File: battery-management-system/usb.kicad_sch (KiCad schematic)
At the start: 2 parts

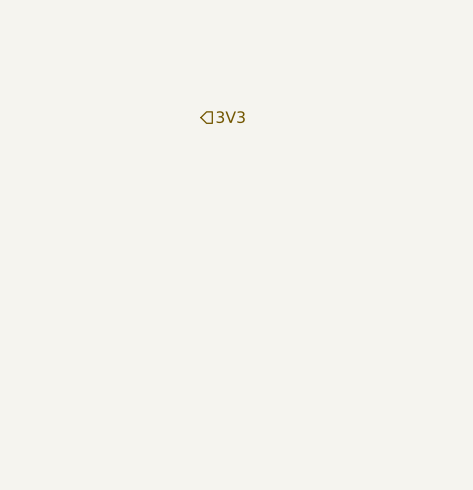
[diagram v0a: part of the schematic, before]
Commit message: define basic hierarchy and power supplies
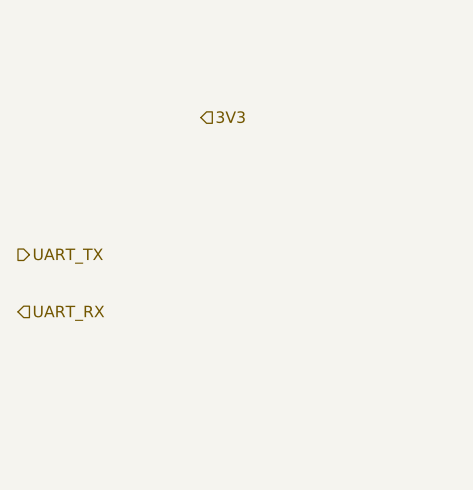
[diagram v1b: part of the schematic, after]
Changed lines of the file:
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@@
 (kicad_sch (version 20211123) (generator eeschema)
   (paper "A4")
+  (hierarchical_label "UART_TX" (shape output) (at 78.74 77.47 0)
+    (effects (font (size 1.27 1.27)) (justify left))
+  )
+  (hierarchical_label "UART_RX" (shape input) (at 78.74 83.82 0)
+    (effects (font (size 1.27 1.27)) (justify left))
+  )
   (hierarchical_label "5V_USB" (shape output) (at 99.06 45.72 0)
     (effects (font (size 1.27 1.27)) (justify left))

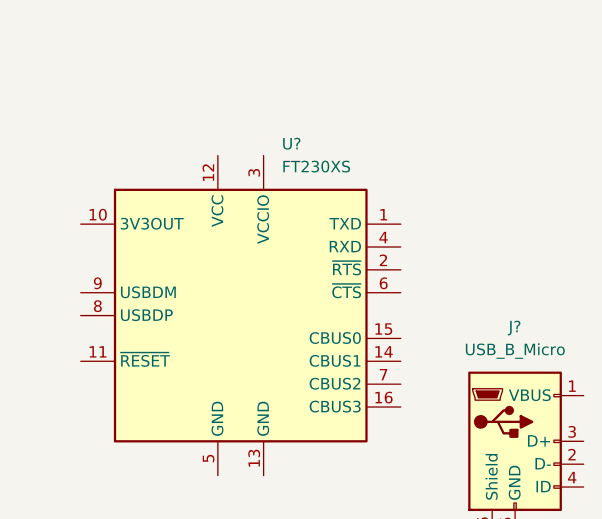
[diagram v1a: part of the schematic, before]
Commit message: add RS order numbers
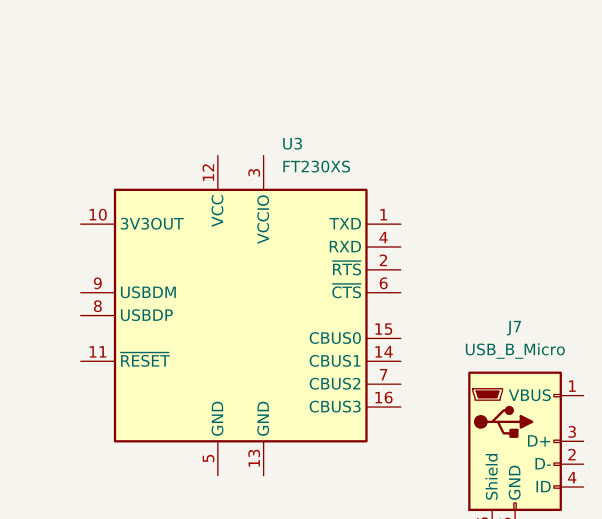
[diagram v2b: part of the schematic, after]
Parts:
- J7: renamed from J?; symbol Connector:USB_B_Micro -> benediktibk:USB_B_Micro
- U3: renamed from U?; symbol Interface_USB:FT230XS -> benediktibk:FT230XS
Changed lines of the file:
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@@
     (effects (font (size 1.27 1.27)) (justify left))
   )
-  (symbol (lib_id "Interface_USB:FT230XS") (at 222.25 77.47 0) (unit 1)
+  (symbol (lib_id "benediktibk:FT230XS") (at 222.25 77.47 0) (unit 1)
     (in_bom yes) (on_board yes) (fields_autoplaced)
-    (property "Reference" "U?" (id 0) (at 226.8094 58.42 0)
+    (property "Reference" "U3" (id 0) (at 226.8094 58.42 0)
       (effects (font (size 1.27 1.27)) (justify left))
     )
@@
     (pin "9")
   )
-  (symbol (lib_id "Connector:USB_B_Micro") (at 252.73 91.44 0) (unit 1)
+  (symbol (lib_id "benediktibk:USB_B_Micro") (at 252.73 91.44 0) (unit 1)
     (in_bom yes) (on_board yes) (fields_autoplaced)
-    (property "Reference" "J?" (id 0) (at 252.73 78.74 0))
+    (property "Reference" "J7" (id 0) (at 252.73 78.74 0))
     (property "Value" "USB_B_Micro" (id 1) (at 252.73 81.28 0))
     (property "Footprint" "" (id 2) (at 256.54 92.71 0)

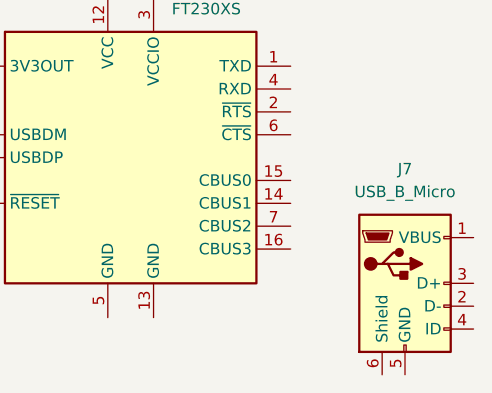
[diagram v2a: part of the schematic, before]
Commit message: add missing order numbers
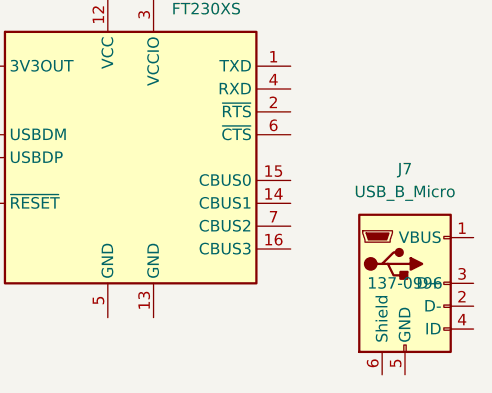
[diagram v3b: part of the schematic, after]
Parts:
- J7: RS order number (none) -> 137-0996
- U3: RS order number (none) -> 757-0010
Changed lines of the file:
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@@
+      (effects (font (size 1.27 1.27)) hide)
+    )
+    (property "RS order number" "757-0010" (id 4) (at 222.25 77.47 0)
       (effects (font (size 1.27 1.27)) hide)
     )
@@
       (effects (font (size 1.27 1.27)) hide)
     )
+    (property "RS order number" "137-0996" (id 4) (at 252.73 91.44 0))
     (pin "1")
     (pin "2")

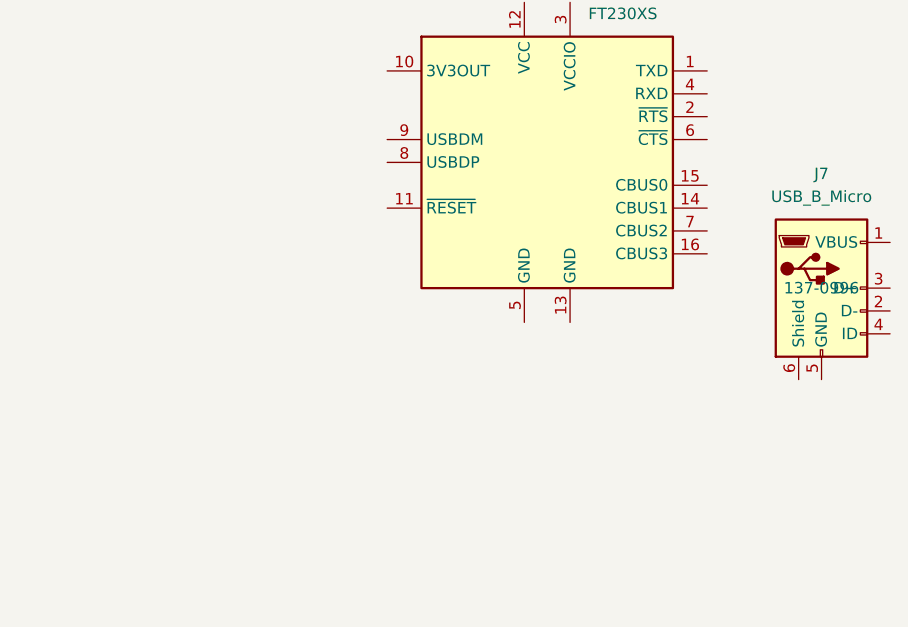
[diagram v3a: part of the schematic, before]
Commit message: use own symbols and footprints
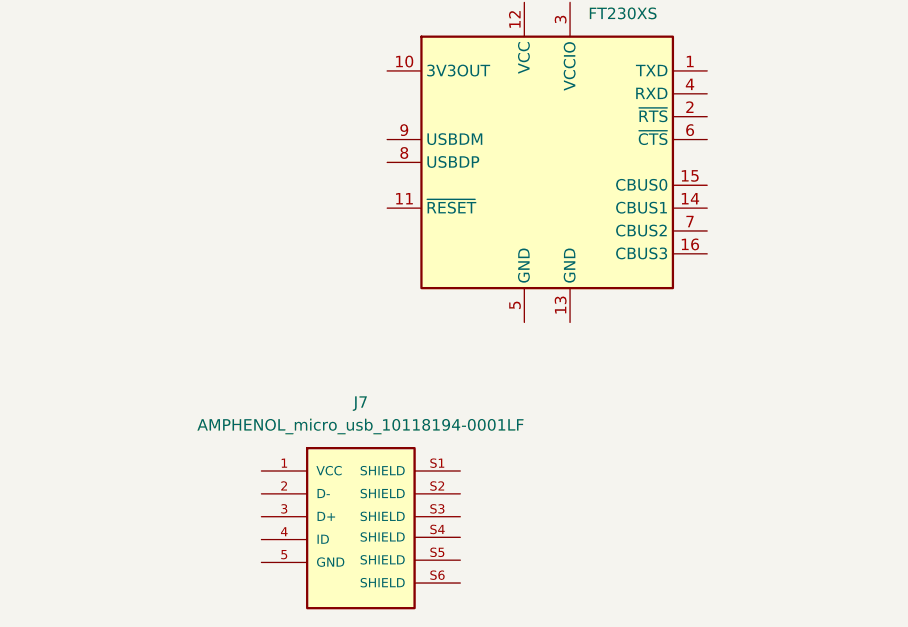
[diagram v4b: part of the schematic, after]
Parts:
- removed J7: USB_B_Micro, symbol benediktibk:USB_B_Micro
- added J7: AMPHENOL_micro_usb_10118194-0001LF, benediktibk:AMPHENOL_10118194-0001LF, symbol benediktibk:AMPHENOL_micro_usb_10118194-0001LF
- U3: footprint Package_SO:SSOP-16_3.9x4.9mm_P0.635mm -> benediktibk:SSOP-16_3.9x4.9mm_P0.635mm
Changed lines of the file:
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@@
       (effects (font (size 1.27 1.27)) (justify left))
     )
-    (property "Footprint" "Package_SO:SSOP-16_3.9x4.9mm_P0.635mm" (id 2) (at 247.65 92.71 0)
+    (property "Footprint" "benediktibk:SSOP-16_3.9x4.9mm_P0.635mm" (id 2) (at 247.65 92.71 0)
       (effects (font (size 1.27 1.27)) hide)
     )
@@
     (pin "9")
   )
-  (symbol (lib_id "benediktibk:USB_B_Micro") (at 252.73 91.44 0) (unit 1)
+  (symbol (lib_id "benediktibk:AMPHENOL_micro_usb_10118194-0001LF") (at 200.66 119.38 0) (unit 1)
     (in_bom yes) (on_board yes) (fields_autoplaced)
-    (property "Reference" "J7" (id 0) (at 252.73 78.74 0))
-    (property "Value" "USB_B_Micro" (id 1) (at 252.73 81.28 0))
-    (property "Footprint" "" (id 2) (at 256.54 92.71 0)
+    (property "Reference" "J7" (id 0) (at 201.549 104.14 0))
+    (property "Value" "AMPHENOL_micro_usb_10118194-0001LF" (id 1) (at 201.549 106.68 0))
+    (property "Footprint" "benediktibk:AMPHENOL_10118194-0001LF" (id 2) (at 201.8792 107.5436 0)
+      (effects (font (size 1.27 1.27)) (justify bottom) hide)
+    )
+    (property "Datasheet" "" (id 3) (at 200.66 119.38 0)
       (effects (font (size 1.27 1.27)) hide)
     )
-    (property "Datasheet" "~" (id 3) (at 256.54 92.71 0)
-      (effects (font (size 1.27 1.27)) hide)
-    )
-    (property "RS order number" "137-0996" (id 4) (at 252.73 91.44 0))
     (pin "1")
     (pin "2")
@@
     (pin "4")
     (pin "5")
-    (pin "6")
+    (pin "S1")
+    (pin "S2")
+    (pin "S3")
+    (pin "S4")
+    (pin "S5")
+    (pin "S6")
   )
 )

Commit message: use M6 connectors, update symbols
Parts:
- J7: RS order number (none) -> 137-0996
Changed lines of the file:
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@@
+      (effects (font (size 1.27 1.27)) hide)
+    )
+    (property "RS order number" "137-0996" (id 4) (at 200.66 119.38 0)
       (effects (font (size 1.27 1.27)) hide)
     )

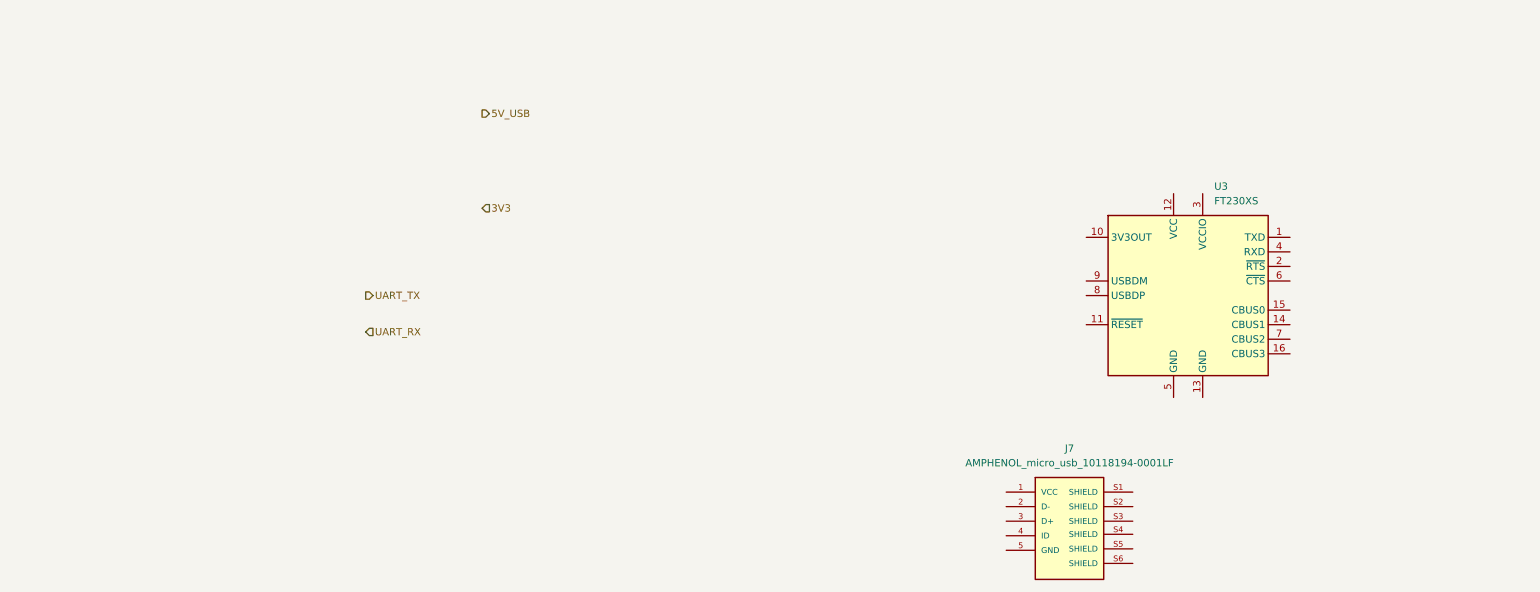
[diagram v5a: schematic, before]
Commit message: create schematic for USB
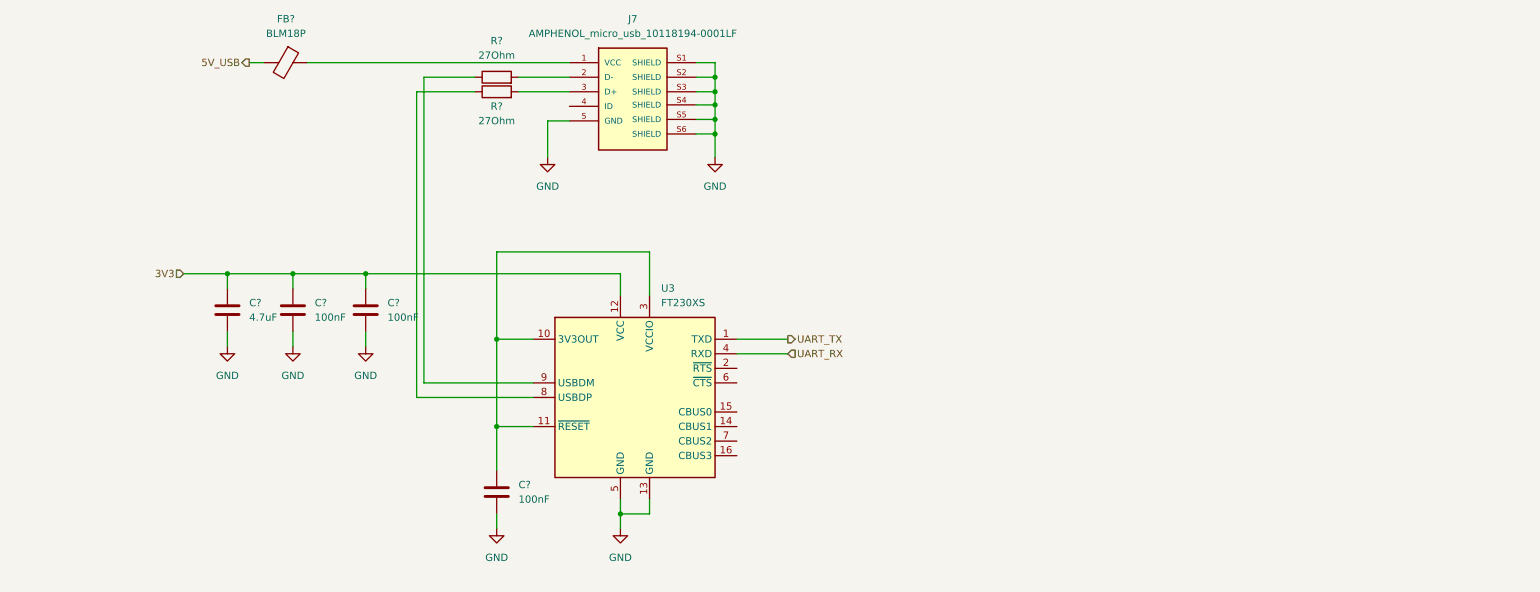
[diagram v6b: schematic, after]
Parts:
- added C? (x3): 100nF, benediktibk:C_0603_1608Metric_Pad1.08x0.95mm_HandSolder, symbol benediktibk:C_100nF_SMD_0603_50V
- added C?: 4.7uF, benediktibk:C_0805_2012Metric_Pad1.18x1.45mm_HandSolder, symbol benediktibk:C_4_7uF_SMD_0805_50V_10%
- added FB?: BLM18P, benediktibk:R_0603_1608Metric_Pad0.98x0.95mm_HandSolder, symbol benediktibk:BLM18P
- added R? (x2): 27Ohm, benediktibk:R_0603_1608Metric_Pad0.98x0.95mm_HandSolder, symbol benediktibk:R_27Ohm_SMD_0603_100mW_1%
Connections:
- net 3V3: now also U3.12 (VCC), C?.1, C?.1, C?.1
- net 5V_USB: now also FB?.2
- net UART_RX: now also U3.4 (RXD)
- net UART_TX: now also U3.1 (TXD)
- net at U3.10 (3V3OUT): now also U3.11 (~{RESET}), U3.3 (VCCIO), C?.1
- net GND: now reaches U3.13 (GND)
- net GND: now also J7.5 (GND), J7.S1 (SHIELD), J7.S2 (SHIELD), J7.S3 (SHIELD), J7.S4 (SHIELD), J7.S5 (SHIELD), J7.S6 (SHIELD), U3.5 (GND), C?.2, C?.2, C?.2, C?.2
- net at U3.8 (USBDP): now also R?.1
- net at U3.9 (USBDM): now also R?.1
- net at J7.1 (VCC): now also FB?.1
- net at J7.2 (D-): now also R?.2
- net at J7.3 (D+): now also R?.2
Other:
- moved on the sheet: J7, U3

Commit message: add resistors, capacitors and LEDs
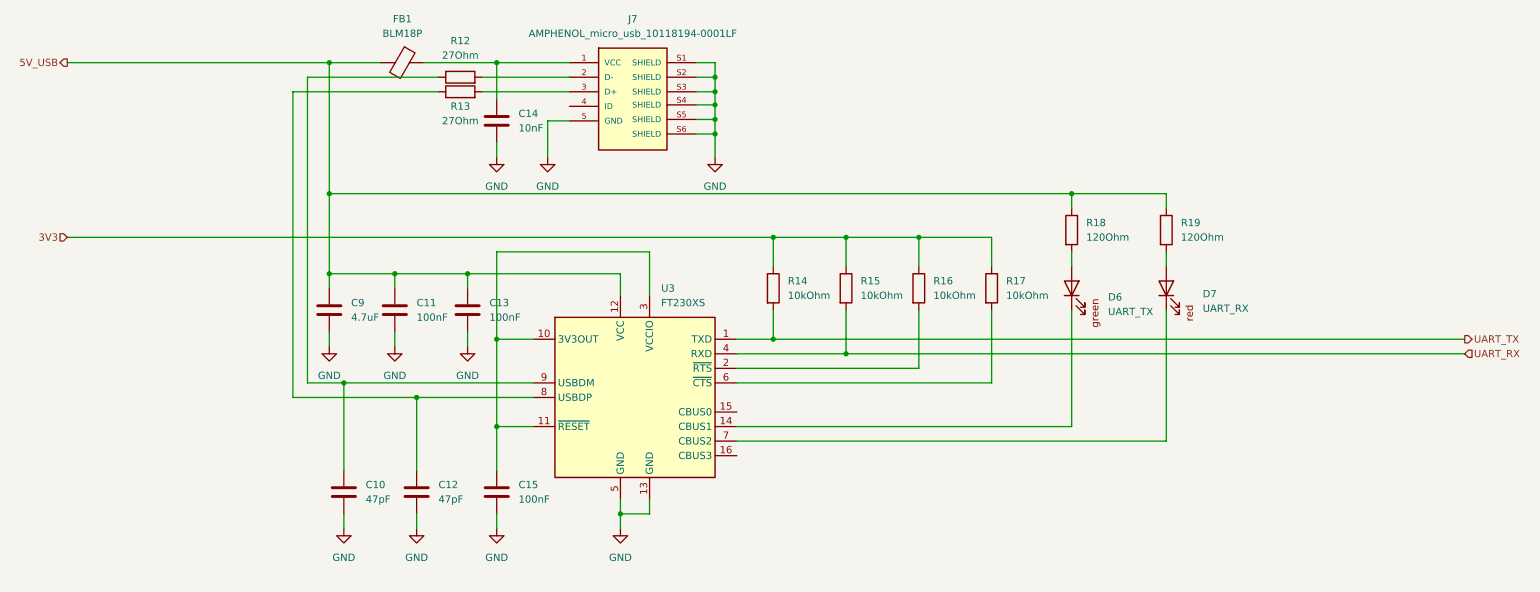
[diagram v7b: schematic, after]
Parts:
- added C10, C12: 47pF, benediktibk:C_0603_1608Metric_Pad1.08x0.95mm_HandSolder, symbol benediktibk:C_47pF_SMD_0603_100V_5%
- added C14: 10nF, benediktibk:C_0603_1608Metric_Pad1.08x0.95mm_HandSolder, symbol benediktibk:C_10nF_SMD_0603_50V_20%
- added D6: UART_TX, benediktibk:D_0603_1608Metric_Pad1.05x0.95mm_HandSolder, symbol benediktibk:LED_green_0603
- added D7: UART_RX, benediktibk:D_0603_1608Metric_Pad1.05x0.95mm_HandSolder, symbol benediktibk:LED_red_0603
- added R14, R15, R16, R17: 10kOhm, benediktibk:R_0603_1608Metric_Pad0.98x0.95mm_HandSolder, symbol benediktibk:R_10kOhm_SMD_0603_100mW_1%
- added R18, R19: 120Ohm, benediktibk:R_0603_1608Metric_Pad0.98x0.95mm_HandSolder, symbol benediktibk:R_120Ohm_SMD_0603_100mW_1%
- gave numbers to parts that had none: 7
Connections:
- net 3V3: now also R14.1, R15.1, R16.1, R17.1; no longer C11.1, C13.1, C9.1, U3.12 (VCC)
- net 5V_USB: now also C11.1, C13.1, C9.1, U3.12 (VCC), R18.1, R19.1
- net GND: now also C10.2, C12.2, C14.2
- net UART_RX: now also R15.2
- net UART_TX: now also R14.2
- net at U3.14 (CBUS1): now also D6.1 (K)
- net at U3.2 (~{RTS}): now also R16.2
- net at U3.6 (~{CTS}): now also R17.2
- net at U3.7 (CBUS2): now also D7.1 (K)
- net at R13.1, U3.8 (USBDP): now also C12.1
- net at R12.1, U3.9 (USBDM): now also C10.1
- net at FB1.1, J7.1 (VCC): now also C14.1
- new net: D7.2 (A), R19.2
- new net: D6.2 (A), R18.2
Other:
- moved on the sheet: C11, C13, C9, FB1, R12, R13
